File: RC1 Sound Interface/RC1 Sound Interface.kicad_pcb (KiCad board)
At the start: 2 copper layers, 99.1 x 83.8 mm, 32 parts, among them J1 Expansion, J2 ADDRESS, U1 74LS138, U2 74LS00, U3 74HC595, U4 74HC595, U5 HM62256BLP-7, U6 74LS244, U7 74LS244, U8 74LS245

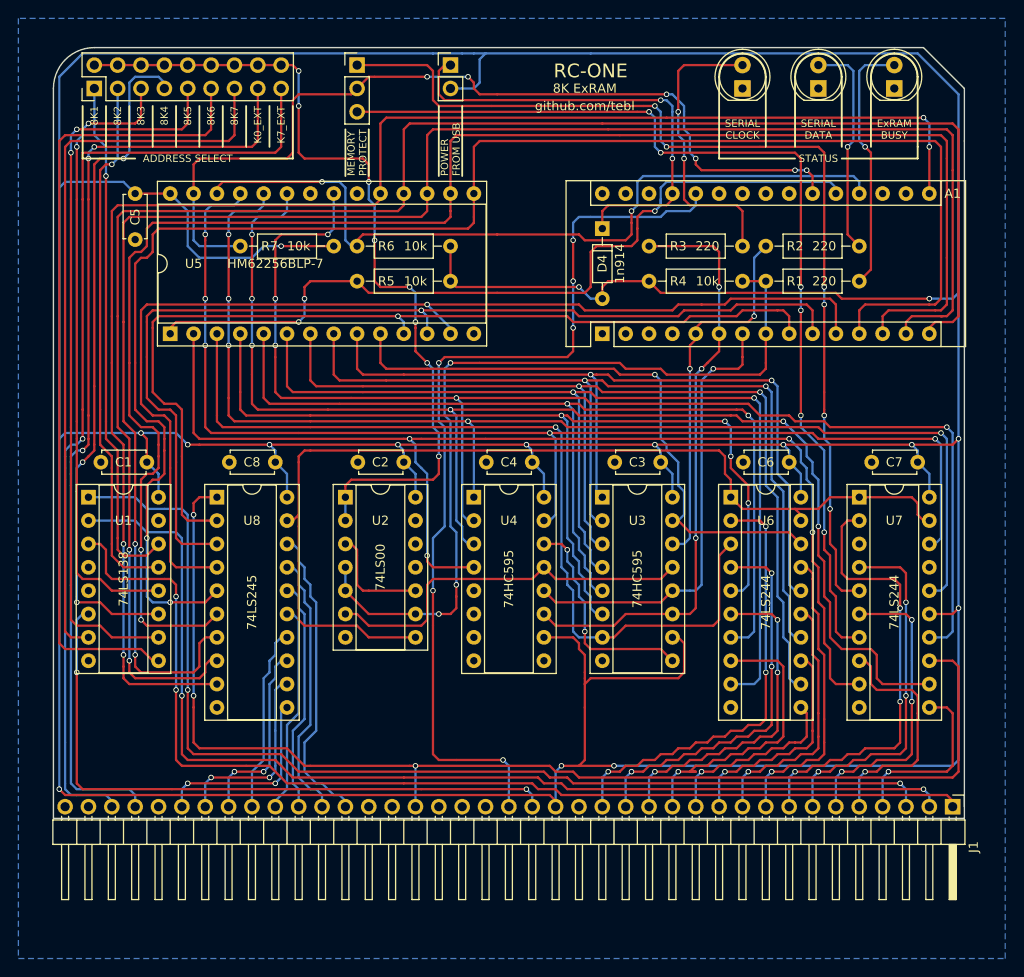
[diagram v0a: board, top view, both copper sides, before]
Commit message: Sound Interface layout done
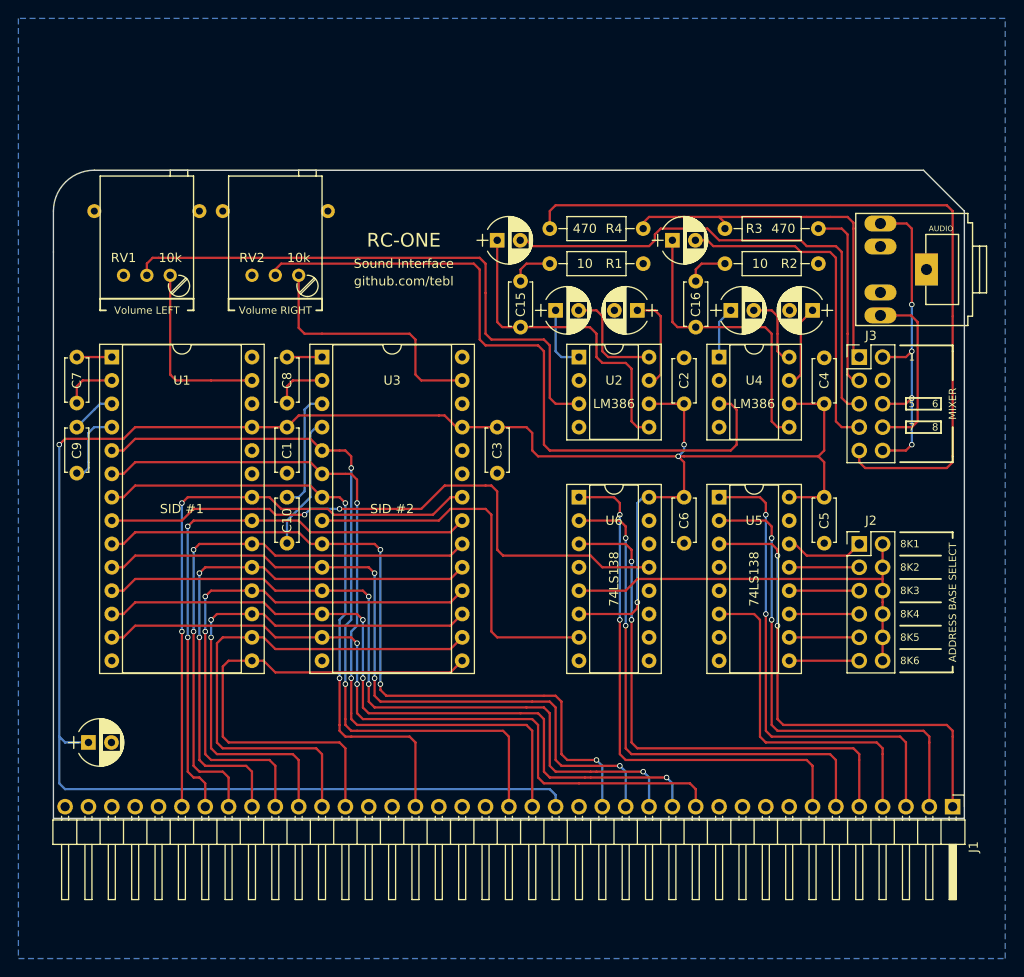
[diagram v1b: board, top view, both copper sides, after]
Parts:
- removed A1: Arduino_Nano_v3.x, Modules:Arduino_Nano
- removed D1: BUSY, LEDs:LED_D5.0mm
- removed D2: DATA, LEDs:LED_D5.0mm
- removed D3: CLK, LEDs:LED_D5.0mm
- removed D4: 1n914, Diodes_THT:D_DO-35_SOD27_P7.62mm_Horizontal
- removed JP1: USB_PWR, Pin_Headers:Pin_Header_Straight_1x02_Pitch2.54mm
- removed JP2: ReadOnly, Pin_Headers:Pin_Header_Straight_1x03_Pitch2.54mm
- removed R5, R6, R7: 10k, Resistors_THT:R_Axial_DIN0207_L6.3mm_D2.5mm_P10.16mm_Horizontal
- removed U7: 74LS244, Housings_DIP:DIP-20_W7.62mm_Socket
- removed U8: 74LS245, Housings_DIP:DIP-20_W7.62mm_Socket
- added C10: 470pF, Capacitors_THT:C_Disc_D4.7mm_W2.5mm_P5.00mm, F.Cu at (120.7, 113.7)
- added C11: 10uF*, Capacitors_THT:CP_Radial_D5.0mm_P2.50mm, F.Cu at (149.9, 93.3)
- added C12: 10uF*, Capacitors_THT:CP_Radial_D5.0mm_P2.50mm, F.Cu at (168.9, 93.3)
- added C13: 10uF*, Capacitors_THT:CP_Radial_D5.0mm_P2.50mm, F.Cu at (158.8, 93.3)
- added C14: 10uF*, Capacitors_THT:CP_Radial_D5.0mm_P2.50mm, F.Cu at (177.8, 93.3)
- added C15: 47nF, Capacitors_THT:C_Disc_D4.7mm_W2.5mm_P5.00mm, F.Cu at (146.1, 90.2)
- added C16: 47nF, Capacitors_THT:C_Disc_D4.7mm_W2.5mm_P5.00mm, F.Cu at (165.1, 90.2)
- added C17: 220uF, Capacitors_THT:CP_Radial_D5.0mm_P2.50mm, F.Cu at (143.5, 85.7)
- added C18: 220uF, Capacitors_THT:CP_Radial_D5.0mm_P2.50mm, F.Cu at (162.6, 85.7)
- added C19: 100uF, Capacitors_THT:CP_Radial_D5.0mm_P2.50mm, F.Cu at (99.1, 140.3)
- added C9: 470pF, Capacitors_THT:C_Disc_D4.7mm_W2.5mm_P5.00mm, F.Cu at (97.8, 106.0)
- added J3: MIXING, Pin_Headers:Pin_Header_Straight_2x05_Pitch2.54mm, F.Cu at (182.9, 98.4)
- added J4: AUDIO, TRS:Tayda_3.5mm_stereo_TRS_jack_A-853, F.Cu at (188.6, 88.9)
- added RV1: 10k, Potentiometer:Potentiometer_Trimmer_Bourns_3296W, F.Cu at (108.0, 89.5)
- added RV2: 10k, Potentiometer:Potentiometer_Trimmer_Bourns_3296W, F.Cu at (121.9, 89.5)
- C7, C8: value 100nF -> 470pF
- J2: footprint Pin_Headers:Pin_Header_Straight_2x09_Pitch2.54mm -> Pin_Headers:Pin_Header_Straight_2x06_Pitch2.54mm
- R1, R2: value 220 -> 10
- R3: value 220 -> 470
- R4: value 10k -> 470
- U1: value 74LS138 -> SID #1; footprint Housings_DIP:DIP-16_W7.62mm_Socket -> Housings_DIP:DIP-28_W15.24mm_Socket
- U2: value 74LS00 -> LM386; footprint Housings_DIP:DIP-14_W7.62mm_Socket -> Housings_DIP:DIP-8_W7.62mm_Socket
- U3: value 74HC595 -> SID #2; footprint Housings_DIP:DIP-16_W7.62mm_Socket -> Housings_DIP:DIP-28_W15.24mm_Socket
- U4: value 74HC595 -> LM386; footprint Housings_DIP:DIP-16_W7.62mm_Socket -> Housings_DIP:DIP-8_W7.62mm_Socket
- U5: value HM62256BLP-7 -> 74LS138; footprint Housings_DIP:DIP-28_W15.24mm_Socket -> Housings_DIP:DIP-16_W7.62mm_Socket
- U6: value 74LS244 -> 74LS138; footprint Housings_DIP:DIP-20_W7.62mm_Socket -> Housings_DIP:DIP-16_W7.62mm_Socket
- moved J2 96.8 mm to (182.9, 118.7), turned to 0 degrees
- moved C7 92.2 mm to (97.8, 98.4), turned to 270 degrees
- moved C5 81.9 mm to (179.1, 113.7)
- moved U5 62.3 mm to (167.6, 113.7), turned to 0 degrees
- moved U3 34.1 mm to (124.5, 98.4)
- moved R1 33.7 mm to (149.2, 88.3), turned to 0 degrees
- moved C4 32.4 mm to (179.1, 103.5), turned to 90 degrees
- moved C2 31.1 mm to (163.8, 103.5), turned to 90 degrees
- moved U4 30.7 mm to (167.6, 98.4)
- moved U2 29.6 mm to (152.4, 98.4)
- moved R4 21.7 mm to (149.2, 84.5), turned to 0 degrees
- moved C3 18.2 mm to (143.5, 106.0), turned to 270 degrees
- moved U6 16.5 mm to (152.4, 113.7)
- moved C1 15.7 mm to (120.7, 106.0), turned to 270 degrees
- moved U1 15.5 mm to (101.6, 98.4)
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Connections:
- C7 pad 1: VCC -> Net-(C7-Pad1)
- C7 pad 2: GND -> Net-(C7-Pad2)
- C8 pad 1: VCC -> Net-(C8-Pad1)
- C8 pad 2: GND -> Net-(C8-Pad2)
- J1 pad 10: /A6 -> (no net)
- J1 pad 11: /A5 -> (no net)
- J1 pad 36: K0_EXT -> (no net)
- J1 pad 37: K7_EXT -> (no net)
- J1 pad 8: /A8 -> (no net)
- J1 pad 9: /A7 -> (no net)
- R1 pad 2: BUS_EN -> GND
- R2 pad 2: SHIFT_DATA -> GND
- R3 pad 2: SHIFT_CLK -> Net-(J3-Pad1)
- R4 pad 1: BUS_EN -> Net-(J3-Pad9)
- R4 pad 2: VCC -> Net-(J3-Pad1)
- U1 pad 1: /A13 -> Net-(C7-Pad1)
- U1 pad 10: /8K5 -> /A1
- U1 pad 11: /8K4 -> /A2
- U1 pad 12: /8K3 -> /A3
- U1 pad 13: /8K2 -> /A4
- U1 pad 14: /8K1 -> GND
- U1 pad 15: (no net) -> /D0
- U1 pad 16: VCC -> /D1
- U1 pad 2: /A14 -> Net-(C7-Pad2)
- U1 pad 3: /A15 -> Net-(C9-Pad1)
- U1 pad 4: GND -> Net-(C9-Pad2)
- U1 pad 5: GND -> /RESET
- U1 pad 7: /8K7 -> /R/~W
- U1 pad 8: GND -> ~SID1
- U1 pad 9: /8K6 -> /A0
- U2 pad 1: Net-(J2-Pad10) -> Net-(C11-Pad1)
- U2 pad 2: Net-(J2-Pad10) -> GND
- U2 pad 3: Net-(U2-Pad10) -> Net-(RV1-Pad2)
- U2 pad 4: BUS_EN -> GND
- U2 pad 5: BUS_EN -> Net-(C15-Pad2)
- U2 pad 6: ~BUS_EN -> VCC
- U2 pad 7: GND -> Net-(C13-Pad1)
- U2 pad 8: ~EXT_CS -> Net-(C11-Pad2)
- U3 pad 1: /EX_A1 -> Net-(C8-Pad1)
- U3 pad 10: VCC -> /A1
- U3 pad 11: SHIFT_CLK -> /A2
- U3 pad 12: SHIFT_LATCH -> /A3
- U3 pad 13: ~BUS_EN -> /A4
- U3 pad 14: SHIFT_DATA -> GND
- U3 pad 15: /EX_A0 -> /D0
- U3 pad 16: VCC -> /D1
- U3 pad 2: /EX_A2 -> Net-(C8-Pad2)
- U3 pad 3: /EX_A3 -> Net-(C10-Pad1)
- U3 pad 4: /EX_A4 -> Net-(C10-Pad2)
- U3 pad 5: /EX_A5 -> /RESET
- U3 pad 6: /EX_A6 -> /PHI2
- U3 pad 7: /EX_A7 -> /R/~W
- U3 pad 8: GND -> ~SID2
- U3 pad 9: Net-(U3-Pad9) -> /A0
- U4 pad 1: /EX_A9 -> Net-(C12-Pad1)
- U4 pad 2: /EX_A10 -> GND
- U4 pad 3: /EX_A11 -> Net-(RV2-Pad2)
- U4 pad 4: /EX_A12 -> GND
- U4 pad 5: (no net) -> Net-(C16-Pad2)
- U4 pad 6: (no net) -> VCC
- U4 pad 7: (no net) -> Net-(C14-Pad1)
- U4 pad 8: GND -> Net-(C12-Pad2)
- U5 pad 1: /EX_A14 -> /A13
- U5 pad 10: /EX_A0 -> /8K5
- U5 pad 11: /EX_D0 -> /8K4
- U5 pad 12: /EX_D1 -> /8K3
- U5 pad 13: /EX_D2 -> /8K2
- U5 pad 14: GND -> /8K1
- U5 pad 15: /EX_D3 -> (no net)
- U5 pad 16: /EX_D4 -> VCC
- U5 pad 2: /EX_A12 -> /A14
- U5 pad 3: /EX_A7 -> /A15
- U5 pad 4: /EX_A6 -> GND
- U5 pad 5: /EX_A5 -> GND
- U5 pad 6: /EX_A4 -> /A12
- U5 pad 7: /EX_A3 -> (no net)
- U5 pad 8: /EX_A2 -> GND
- U5 pad 9: /EX_A1 -> /8K6
- U6 pad 1: ~EXT_CS -> /A9
- U6 pad 10: GND -> (no net)
- U6 pad 11: /A4 -> (no net)
- U6 pad 12: /EX_A3 -> (no net)
- U6 pad 13: /A5 -> ~SID1
- U6 pad 14: /EX_A2 -> (no net)
- U6 pad 15: /A6 -> (no net)
- U6 pad 16: /EX_A1 -> VCC
- U6 pad 2: /A0 -> /A10
- U6 pad 3: /EX_A7 -> /A11
- U6 pad 4: /A1 -> GND
- U6 pad 5: /EX_A6 -> Net-(J2-Pad10)
- U6 pad 6: /A2 -> VCC
- U6 pad 7: /EX_A5 -> ~SID2
- U6 pad 8: /A3 -> GND
- U6 pad 9: /EX_A4 -> (no net)
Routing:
- net VCC: track 643.1 -> 239.0 mm, vias 16 -> 4
- net /EX_D6: track 187.2 -> 0.00 mm, vias 2 -> 0
- net /EX_D5: track 186.6 -> 0.00 mm, vias 2 -> 0
- net /EX_D4: track 179.5 -> 0.00 mm, vias 2 -> 0
- net /EX_D3: track 175.7 -> 0.00 mm, vias 2 -> 0
- net /EX_D7: track 167.6 -> 0.00 mm, vias 4 -> 0
- net /EX_A10: track 141.6 -> 0.00 mm, vias 5 -> 0
- net /EX_A11: track 140.5 -> 0.00 mm, vias 6 -> 0
- net /EX_A9: track 132.9 -> 0.00 mm, vias 5 -> 0
- net /EX_A8: track 131.6 -> 0.00 mm, vias 5 -> 0
- net /EX_A12: track 126.6 -> 0.00 mm, vias 4 -> 0
- net /EX_D2: track 119.0 -> 0.00 mm, vias 1 -> 0
- net /EX_A4: track 112.6 -> 0.00 mm, vias 2 -> 0
- net ~EXT_CS: track 110.4 -> 0.00 mm
- net /EX_D1: track 109.9 -> 0.00 mm, vias 1 -> 0
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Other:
- board size 99.1 x 83.8 mm -> 99.1 x 70.5 mm
- board text added: "$2400"
- board text added: "$2E00"
- board text added: "$4400"
- board text added: "$4E00"
- board text added: "$6400"
- board text added: "$6E00"
- board text added: "$8400"
- board text added: "$8E00"
- board text added: "$A400"
- board text added: "$AE00"
- board text added: "$C400"
- board text added: "$CE00"
- board text added: "$x400 - $x41C"
- board text added: "$x400 = SID#1 $xE00 = SID#2"
- board text added: "$xE00 - $xE1C"
- board text added: "$xx00 $xx01 $xx02 $xx03 $xx04 $xx05 $xx06"
- board text added: "$xx07 $xx08 $xx09 $xx0A $xx0B $xx0C $xx0D"
- board text added: "$xx0E $xx0F $xx10 $xx11 $xx12 $xx13 $xx14"
- board text added: "$xx15 $xx16 $xx17 $xx18 $xx1B $xx1C"
- board text added: "1"
- board text added: "10"
- board text added: "2"
- board text added: "3"
- board text added: "5"
- board text added: "6"
- board text added: "7"
- board text added: "8"
- board text added: "9"
- board text added: "ADDRESS BASE SELECT"
- board text added: "ADDRESS DECODING"
- board text added: "DOWNMIX STEREO"
- board text added: "Filt. cutoff freq. LB Filt. cutoff freq. HB Filt. resonance/routing Filt. mode/volume V3 oscillator V3 envelope"
- board text added: "MIXER"
- board text added: "MONO"
- board text added: "SID #1"
- board text added: "SID #1 AMPLIFIER"
- board text added: "SID #2"
- board text added: "SID #2 AMPLIFIER"
- board text added: "STEREO"
- board text added: "Sound Interface"
- board text added: "V1 freq. LB V1 freq. HB V1 Pulse wave LB V1 Pulse wave HB V1 Control V1 attack/decay V1 sustain/release"
- board text added: "V2 freq. LB V2 freq. HB V2 Pulse wave LB V2 Pulse wave HB V2 Control V2 attack/decay V2 sustain/release"
- board text added: "V3 freq. LB V3 freq. HB V3 Pulse wave LB V3 Pulse wave HB V3 Control V3 attack/decay V3 sustain/release"
- board text added: "Volume LEFT"
- board text added: "Volume RIGHT"
- board text removed: "$2000-"
- board text removed: "$3FFF"
- board text removed: "$4000-"
- board text removed: "$5FFF"
- board text removed: "$6000-"
- board text removed: "$7FFF"
- board text removed: "$8000-"
- board text removed: "$9FFF"
- board text removed: "$A000-"
- board text removed: "$BFFF"
- board text removed: "$C000-"
- board text removed: "$DFFF"
- board text removed: "$E000-"
- board text removed: "$FFFF"
- board text removed: "8K ExRAM"
- board text removed: "8K7"
- board text removed: "ADDRESS SELECT"
- board text removed: "DISABLE"
- board text removed: "ENABLE"
- board text removed: "ExRAM BUSY"
- board text removed: "FROM USB"
- board text removed: "K0_EXT"
- board text removed: "K7_EXT"
- board text removed: "MEMORY"
- board text removed: "POWER"
- board text removed: "PROTECT"
- board text removed: "SELECT"
- board text removed: "SERIAL CLOCK"
- board text removed: "SERIAL DATA"
- board text removed: "STATUS"

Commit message: Address calculations fixed
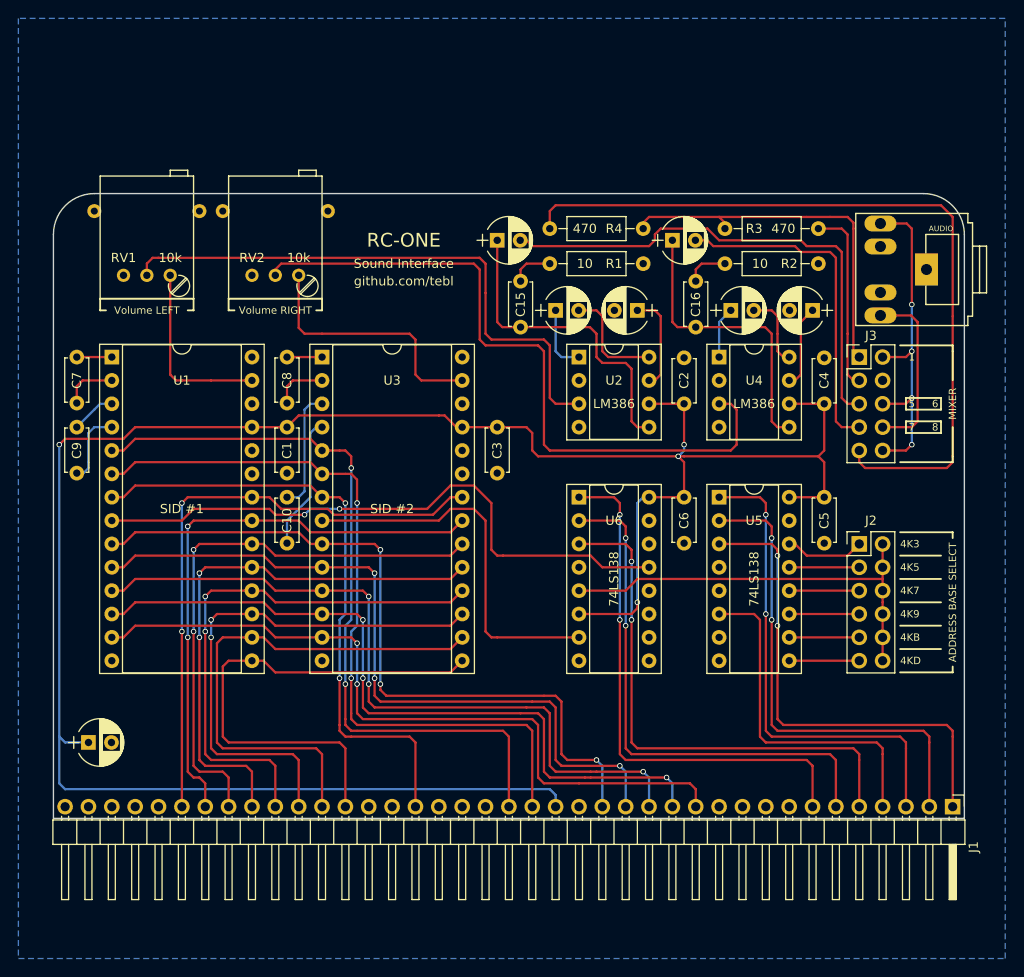
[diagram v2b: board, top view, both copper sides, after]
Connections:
- net /8K1 renamed /4K3
- net /8K2 renamed /4K5
- net /8K3 renamed /4K7
- net /8K4 renamed /4K9
- net /8K5 renamed /4KB
- net /8K6 renamed /4KD
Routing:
- net ~SID1: track 67.9 -> 67.2 mm
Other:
- board size 99.1 x 70.5 mm -> 99.1 x 67.9 mm
- board text added: "$3400"
- board text added: "$3E00"
- board text added: "$5400"
- board text added: "$5E00"
- board text added: "$7400"
- board text added: "$7E00"
- board text added: "$9400"
- board text added: "$9E00"
- board text added: "$B400"
- board text added: "$BE00"
- board text added: "$D400"
- board text added: "$DE00"
- board text added: "4K3"
- board text added: "4K5"
- board text added: "4K7"
- board text added: "4K9"
- board text added: "4KB"
- board text added: "4KD"
- board text added: "Revision B"
- board text removed: "$2400"
- board text removed: "$2E00"
- board text removed: "$4400"
- board text removed: "$4E00"
- board text removed: "$6400"
- board text removed: "$6E00"
- board text removed: "$8400"
- board text removed: "$8E00"
- board text removed: "$A400"
- board text removed: "$AE00"
- board text removed: "$C400"
- board text removed: "$CE00"
- board text removed: "8K1"
- board text removed: "8K2"
- board text removed: "8K3"
- board text removed: "8K4"
- board text removed: "8K5"
- board text removed: "8K6"
- board text removed: "Revision A"
